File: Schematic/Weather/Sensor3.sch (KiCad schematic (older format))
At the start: 2 parts, among them J26 Conn_01x04_Male

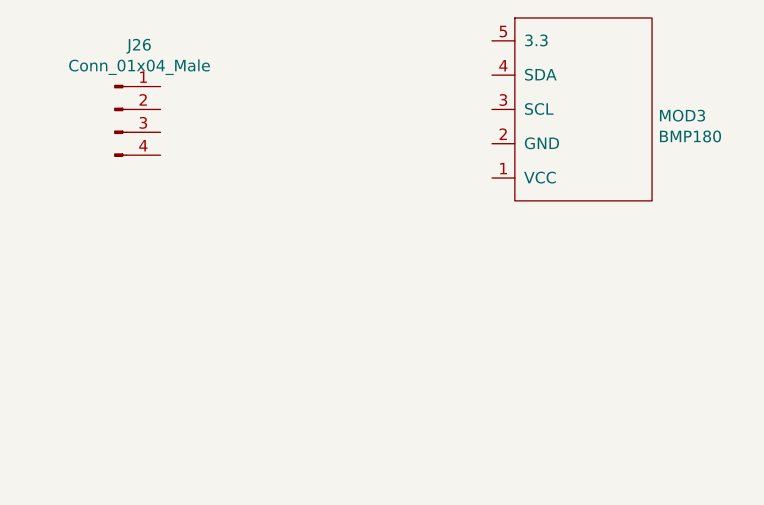
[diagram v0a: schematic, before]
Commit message: Connector relable start
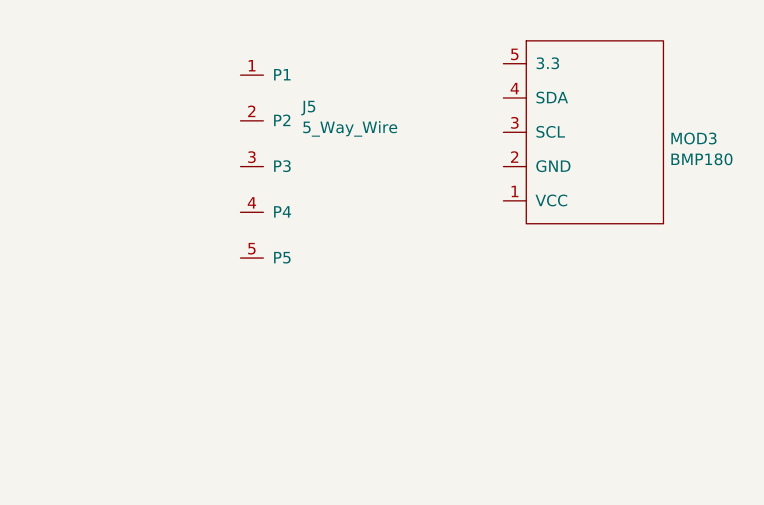
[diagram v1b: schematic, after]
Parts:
- removed J26: Conn_01x04_Male, Connector_PinHeader_2.54mm:PinHeader_1x04_P2.54mm_Vertical, symbol Connector:Conn_01x04_Male
- added J5: 5_Way_Wire, symbol MyComponents:5_Way_Wire
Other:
- moved on the sheet: MOD3
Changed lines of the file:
@@
 $Descr A4 11693 8268
 encoding utf-8
-Sheet 15 15
+Sheet 14 15
 Title ""
 Date ""
@@
 L MyComponents:BMP180 MOD3
 U 1 1 5CB3BC30
-P 6150 2400
-F 0 "MOD3" H 6778 2321 50  0000 L CNN
-F 1 "BMP180" H 6778 2230 50  0000 L CNN
-F 2 "footprint:BMP180" H 6350 1900 50  0001 C CNN
-F 3 "" H 6350 1900 50  0001 C CNN
-	1    6150 2400
+P 6200 2500
+F 0 "MOD3" H 6828 2421 50  0000 L CNN
+F 1 "BMP180" H 6828 2330 50  0000 L CNN
+F 2 "footprint:BMP180" H 6400 2000 50  0001 C CNN
+F 3 "" H 6400 2000 50  0001 C CNN
+	1    6200 2500
 	1    0    0    -1
 $EndComp
 $Comp
-L Connector:Conn_01x04_Male J26
-U 1 1 5CB3C4D7
-P 4400 2450
-F 0 "J26" H 4508 2731 50  0000 C CNN
-F 1 "Conn_01x04_Male" H 4508 2640 50  0000 C CNN
-F 2 "Connector_PinHeader_2.54mm:PinHeader_1x04_P2.54mm_Vertical" H 4400 2450 50  0001 C CNN
-F 3 "~" H 4400 2450 50  0001 C CNN
-	1    4400 2450
+L MyComponents:5_Way_Wire J5
+U 1 1 5CAF5E59
+P 5050 2300
+F 0 "J5" H 5219 2161 50  0000 L CNN
+F 1 "5_Way_Wire" H 5219 2070 50  0000 L CNN
+F 2 "" H 5050 2300 50  0001 C CNN
+F 3 "" H 5050 2300 50  0001 C CNN
+	1    5050 2300
 	1    0    0    -1
 $EndComp

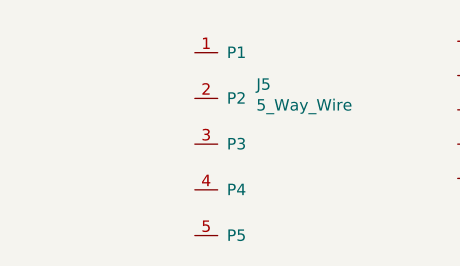
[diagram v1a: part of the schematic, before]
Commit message: Connector changes
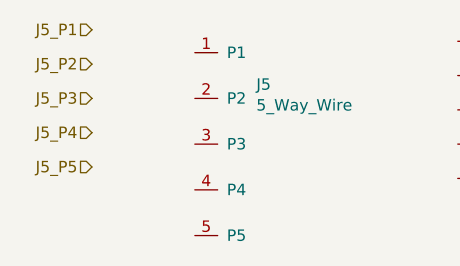
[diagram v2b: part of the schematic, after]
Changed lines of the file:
@@
 $Descr A4 11693 8268
 encoding utf-8
-Sheet 14 15
+Sheet 12 15
 Title ""
 Date ""
@@
 	1    0    0    -1
 $EndComp
+Text HLabel 4500 2200 0    50   Input ~ 0
+J5_P1
+Text HLabel 4500 2350 0    50   Input ~ 0
+J5_P2
+Text HLabel 4500 2500 0    50   Input ~ 0
+J5_P3
+Text HLabel 4500 2650 0    50   Input ~ 0
+J5_P4
+Text HLabel 4500 2800 0    50   Input ~ 0
+J5_P5
 $EndSCHEMATC

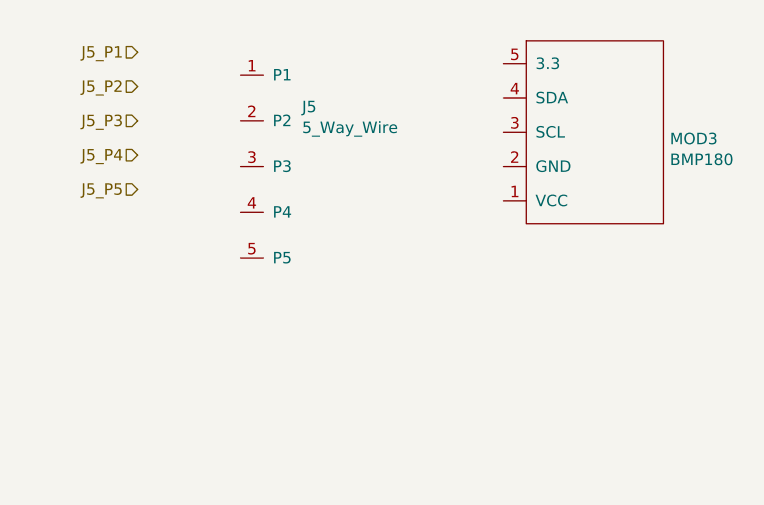
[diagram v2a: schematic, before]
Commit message: config connectors sda scl
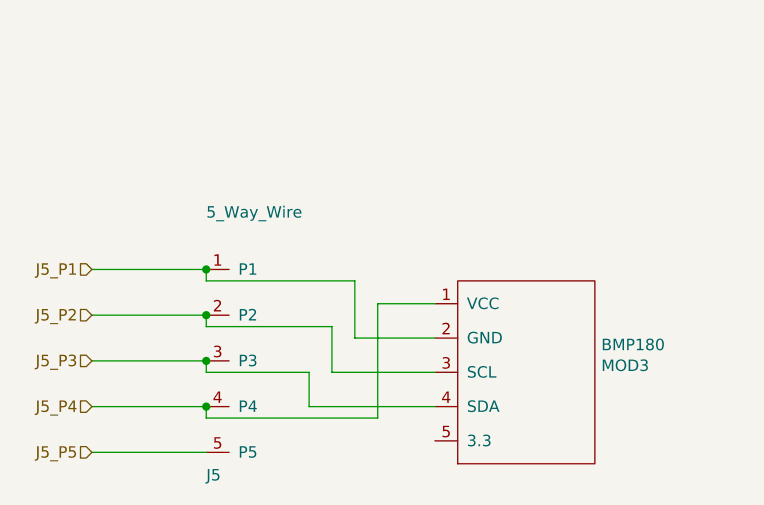
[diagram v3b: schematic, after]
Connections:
- net J5_P1: now also J5.1 (P1), MOD3.2 (GND)
- net J5_P2: now also J5.2 (P2), MOD3.3 (SCL)
- net J5_P3: now also J5.3 (P3), MOD3.4 (SDA)
- net J5_P4: now also J5.4 (P4), MOD3.1 (VCC)
- net J5_P5: now also J5.5 (P5)
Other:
- moved on the sheet: J5, MOD3
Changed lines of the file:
@@
 L MyComponents:BMP180 MOD3
 U 1 1 5CB3BC30
-P 6200 2500
-F 0 "MOD3" H 6828 2421 50  0000 L CNN
-F 1 "BMP180" H 6828 2330 50  0000 L CNN
-F 2 "footprint:BMP180" H 6400 2000 50  0001 C CNN
-F 3 "" H 6400 2000 50  0001 C CNN
-	1    6200 2500
-	1    0    0    -1
+P 5900 3650
+F 0 "MOD3" H 6528 3571 50  0000 L CNN
+F 1 "BMP180" H 6528 3480 50  0000 L CNN
+F 2 "footprint:BMP180" H 6100 3150 50  0001 C CNN
+F 3 "" H 6100 3150 50  0001 C CNN
+	1    5900 3650
+	1    0    0    1
 $EndComp
+Text HLabel 4300 3150 0    50   Input ~ 0
+J5_P1
+Text HLabel 4300 3350 0    50   Input ~ 0
+J5_P2
+Text HLabel 4300 3550 0    50   Input ~ 0
+J5_P3
+Text HLabel 4300 3750 0    50   Input ~ 0
+J5_P4
+Text HLabel 4300 3950 0    50   Input ~ 0
+J5_P5
+Wire Wire Line
+	4300 3150 4800 3150
+Wire Wire Line
+	4300 3350 4800 3350
+Wire Wire Line
+	4300 3550 4800 3550
+Wire Wire Line
+	4300 3750 4800 3750
+Wire Wire Line
+	4300 3950 4800 3950
 $Comp
 L MyComponents:5_Way_Wire J5
 U 1 1 5CAF5E59
-P 5050 2300
-F 0 "J5" H 5219 2161 50  0000 L CNN
-F 1 "5_Way_Wire" H 5219 2070 50  0000 L CNN
-F 2 "" H 5050 2300 50  0001 C CNN
-F 3 "" H 5050 2300 50  0001 C CNN
-	1    5050 2300
+P 4900 3150
+F 0 "J5" H 4800 2250 50  0000 L CNN
+F 1 "5_Way_Wire" H 4800 3400 50  0000 L CNN
+F 2 "" H 4900 3150 50  0001 C CNN
+F 3 "" H 4900 3150 50  0001 C CNN
+	1    4900 3150
 	1    0    0    -1
 $EndComp
-Text HLabel 4500 2200 0    50   Input ~ 0
-J5_P1
-Text HLabel 4500 2350 0    50   Input ~ 0
-J5_P2
-Text HLabel 4500 2500 0    50   Input ~ 0
-J5_P3
-Text HLabel 4500 2650 0    50   Input ~ 0
-J5_P4
-Text HLabel 4500 2800 0    50   Input ~ 0
-J5_P5
+Wire Wire Line
+	5800 3750 5250 3750
+Wire Wire Line
+	5250 3750 5250 3600
+Wire Wire Line
+	5250 3600 4800 3600
+Wire Wire Line
+	4800 3600 4800 3550
+Connection ~ 4800 3550
+Wire Wire Line
+	5800 3600 5350 3600
+Wire Wire Line
+	5350 3600 5350 3400
+Wire Wire Line
+	5350 3400 4800 3400
+Wire Wire Line
+	4800 3400 4800 3350
+Connection ~ 4800 3350
+Wire Wire Line
+	5800 3450 5450 3450
+Wire Wire Line
+	5450 3450 5450 3200
+Wire Wire Line
+	5450 3200 4800 3200
+Wire Wire Line
+	4800 3200 4800 3150
+Connection ~ 4800 3150
+Wire Wire Line
+	5800 3300 5550 3300
+Wire Wire Line
+	5550 3300 5550 3800
+Wire Wire Line
+	5550 3800 4800 3800
+Wire Wire Line
+	4800 3800 4800 3750
+Connection ~ 4800 3750
 $EndSCHEMATC

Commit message: Local webpage added
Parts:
- J5: footprint (none) -> Connector_PinSocket_2.54mm:PinSocket_1x05_P2.54mm_Vertical
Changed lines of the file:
@@
 F 0 "J5" H 4800 2250 50  0000 L CNN
 F 1 "5_Way_Wire" H 4800 3400 50  0000 L CNN
-F 2 "" H 4900 3150 50  0001 C CNN
+F 2 "Connector_PinSocket_2.54mm:PinSocket_1x05_P2.54mm_Vertical" H 4900 3150 50  0001 C CNN
 F 3 "" H 4900 3150 50  0001 C CNN
 	1    4900 3150
